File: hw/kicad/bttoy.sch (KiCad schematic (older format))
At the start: 29 parts

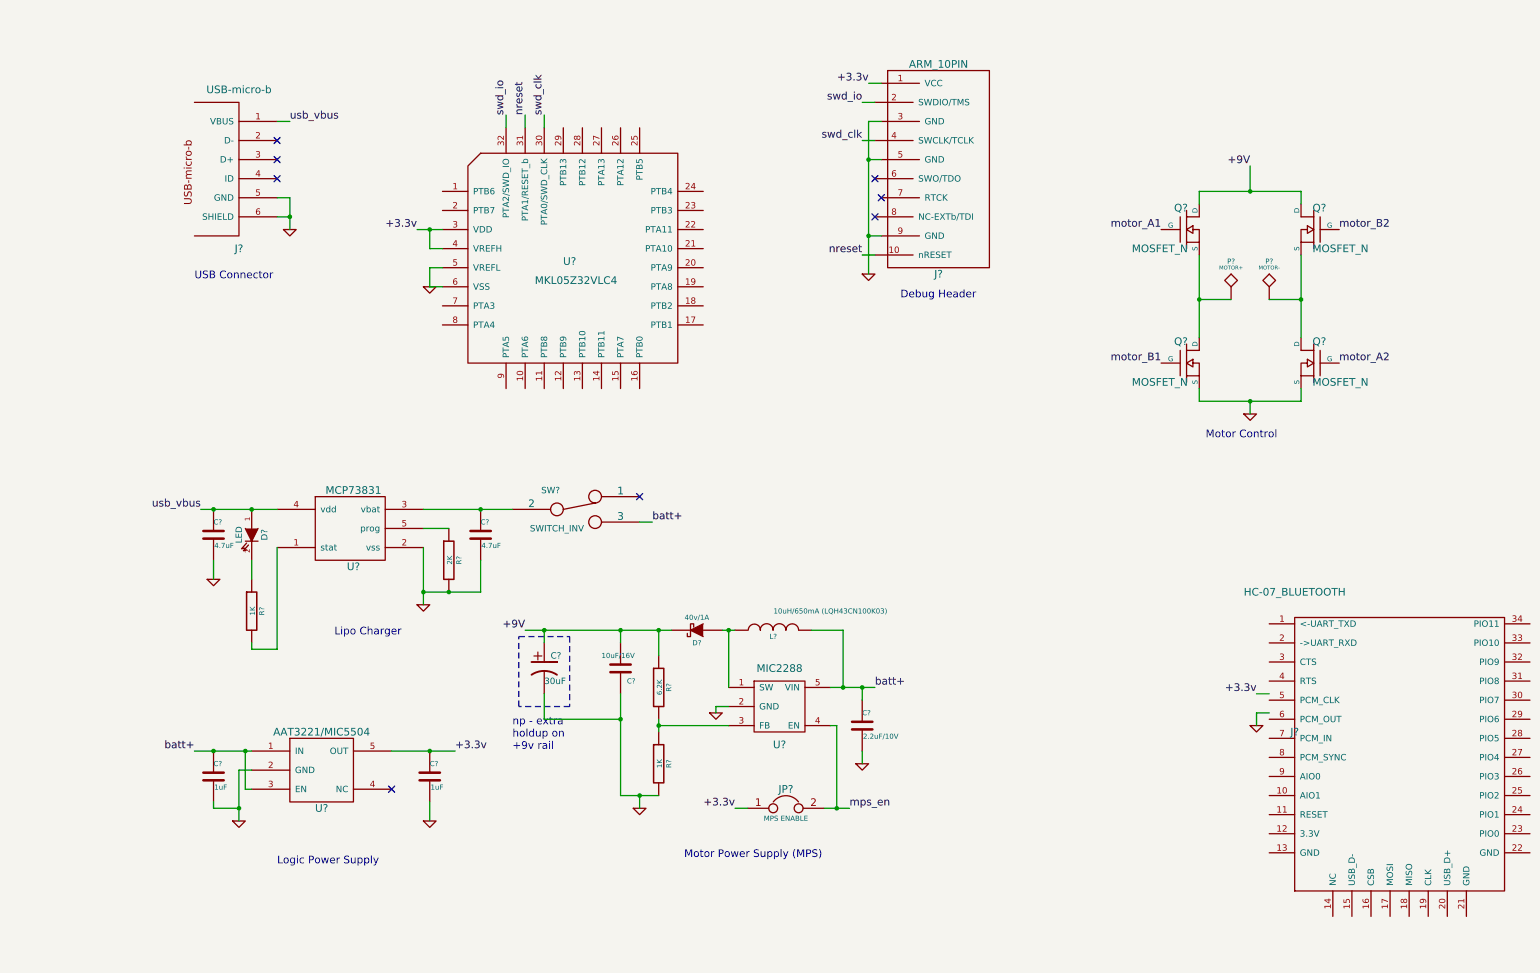
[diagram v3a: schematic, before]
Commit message: - change high side switches to pfet
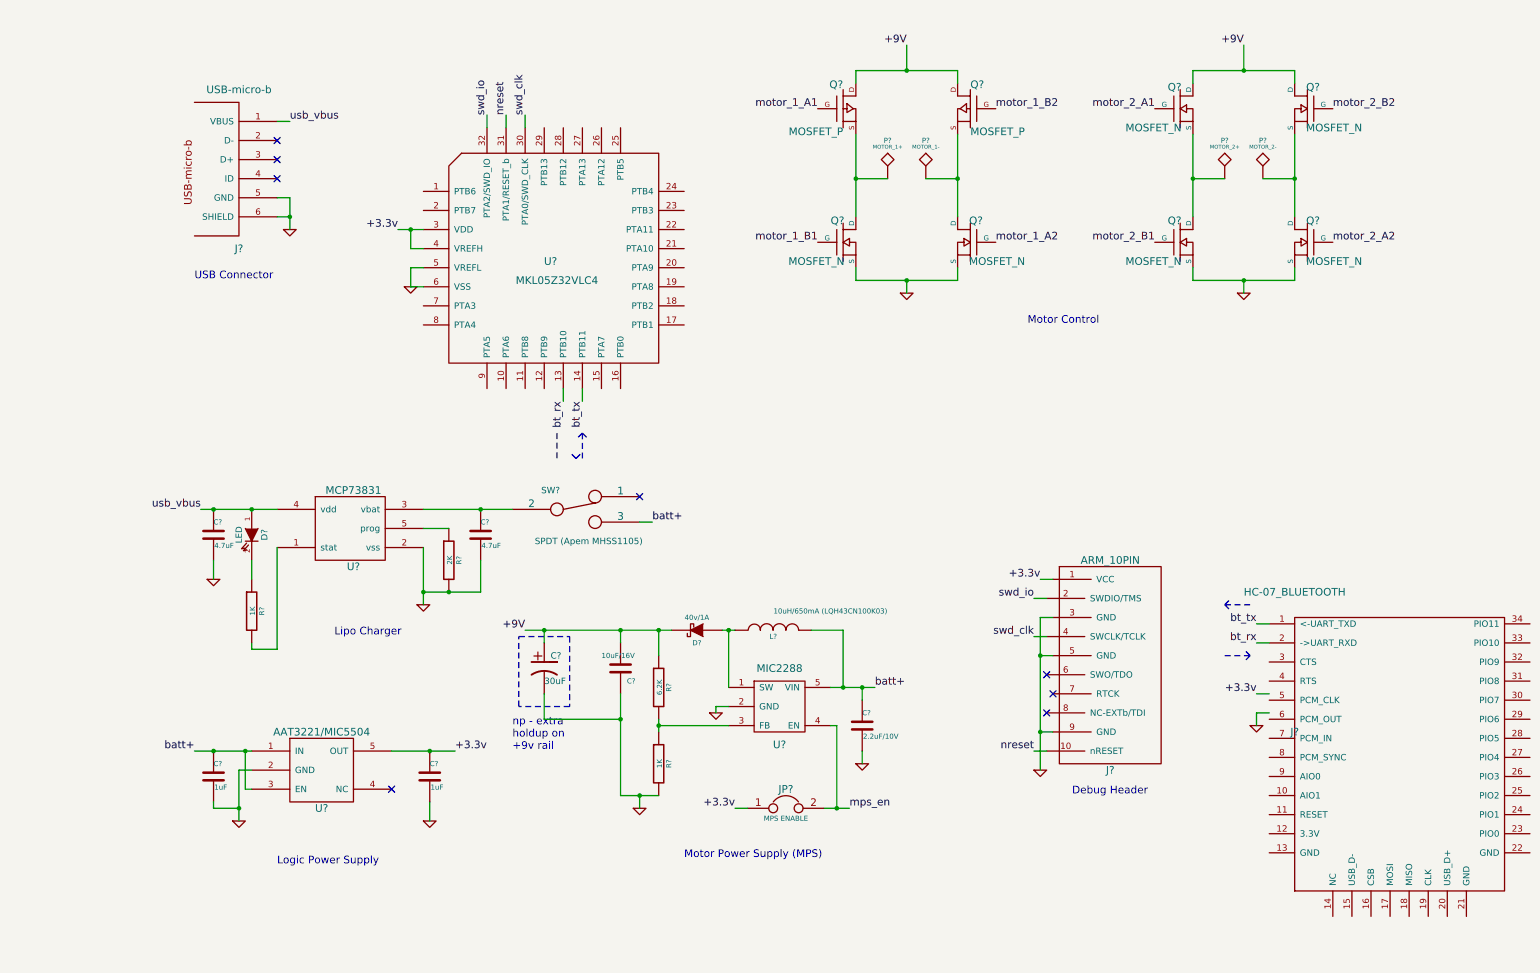
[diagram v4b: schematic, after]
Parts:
- added P?: MOTOR_1+, symbol TST
- added P?: MOTOR_1-, symbol TST
- added Q? (x2): MOSFET_N, symbol MOSFET_N
- added Q? (x2): MOSFET_P, symbol MOSFET_P
- P?: value MOTOR+ -> MOTOR_2+
- P?: value MOTOR- -> MOTOR_2-
- SW?: value SWITCH_INV -> SPDT (Apem MHSS1105)
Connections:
- net +9V: now also Q?.D, Q?.D
- net GND: now also Q?.S, Q?.S
- net bt_rx: now reaches U?.13 (PTB10)
- net bt_rx: now also J?.2 (->UART_RXD)
- net bt_tx: now reaches U?.14 (PTB11)
- net bt_tx: now also J?.1 (<-UART_TXD)
- net motor_A1 renamed motor_2_A1
- net motor_A2 renamed motor_2_A2
- net motor_B1 renamed motor_2_B1
- net motor_B2 renamed motor_2_B2
- new net: P?.1, Q?.D, Q?.S (x2)
- new net motor_1_A1: Q?.G
- new net motor_1_A2: Q?.G
- new net motor_1_B1: Q?.G
- new net motor_1_B2: Q?.G
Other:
- moved on the sheet: J?, P?, Q?, U?

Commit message: - remove sub schematic, replace discrete motor control with LV8548 IC
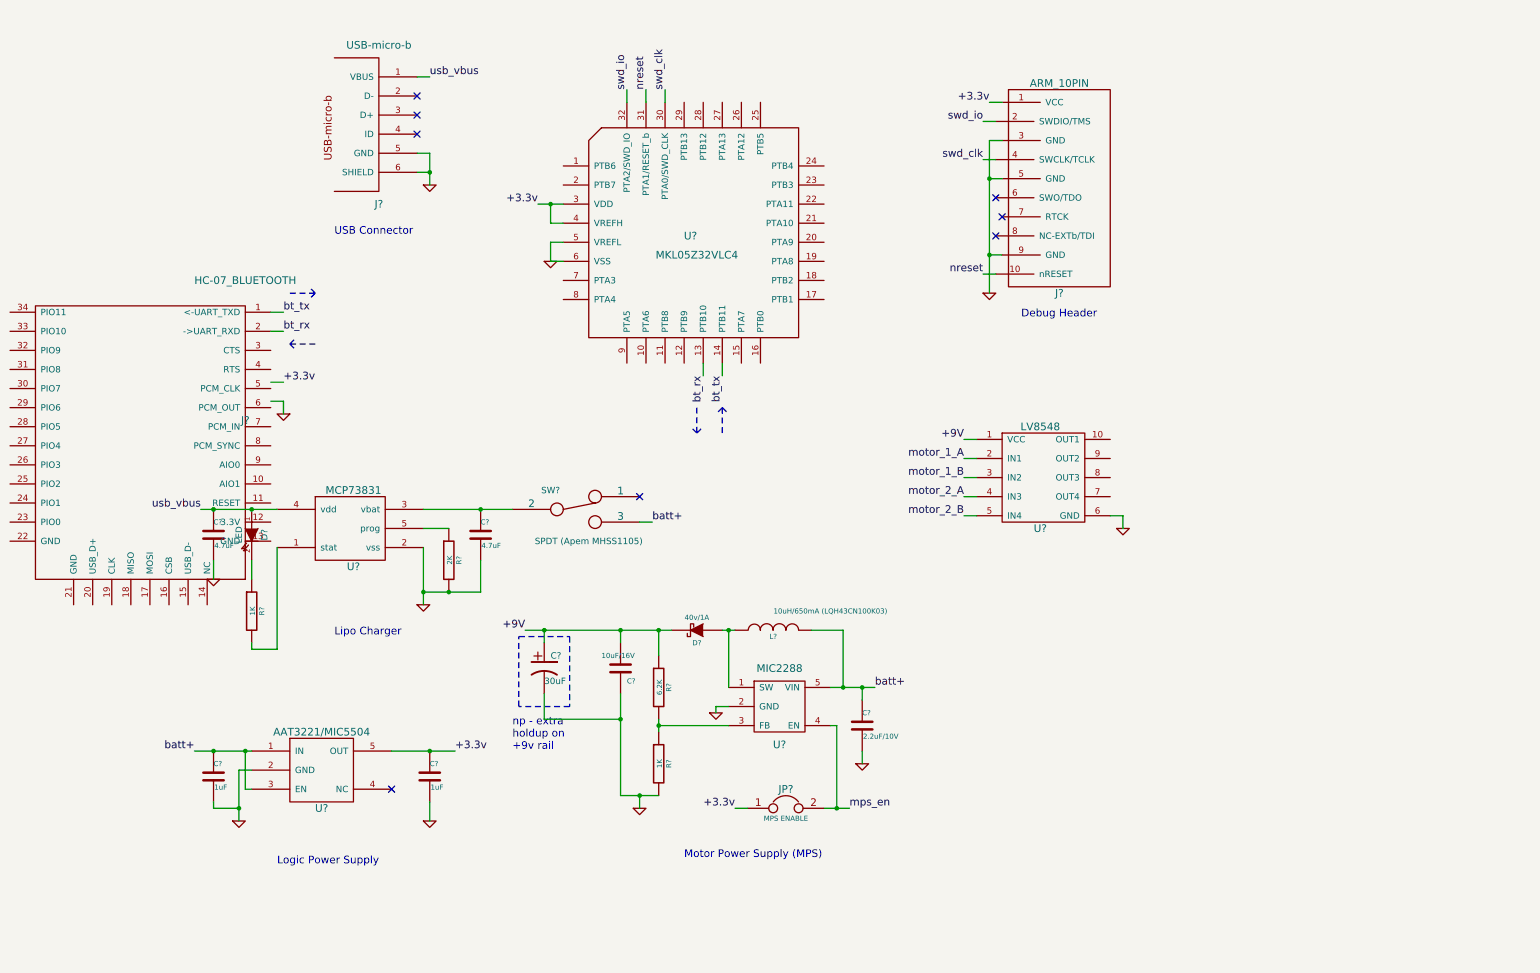
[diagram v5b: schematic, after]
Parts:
- removed P?: MOTOR_2+, symbol TST
- removed P?: MOTOR_2-, symbol TST
- removed P?: MOTOR_1+, symbol TST
- removed P?: MOTOR_1-, symbol TST
- removed Q? (x6): MOSFET_N, symbol MOSFET_N
- removed Q? (x2): MOSFET_P, symbol MOSFET_P
- added U?: LV8548, symbol LV8548
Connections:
- net +9V: now also U?.1 (VCC)
- net GND: now also U?.6 (GND)
- new net motor_1_A: U?.2 (IN1)
- new net motor_1_B: U?.3 (IN2)
- new net motor_2_A: U?.4 (IN3)
- new net motor_2_B: U?.5 (IN4)
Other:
- note removed: "Motor Control"
- moved on the sheet: J?, U?

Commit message: - add motor connectors
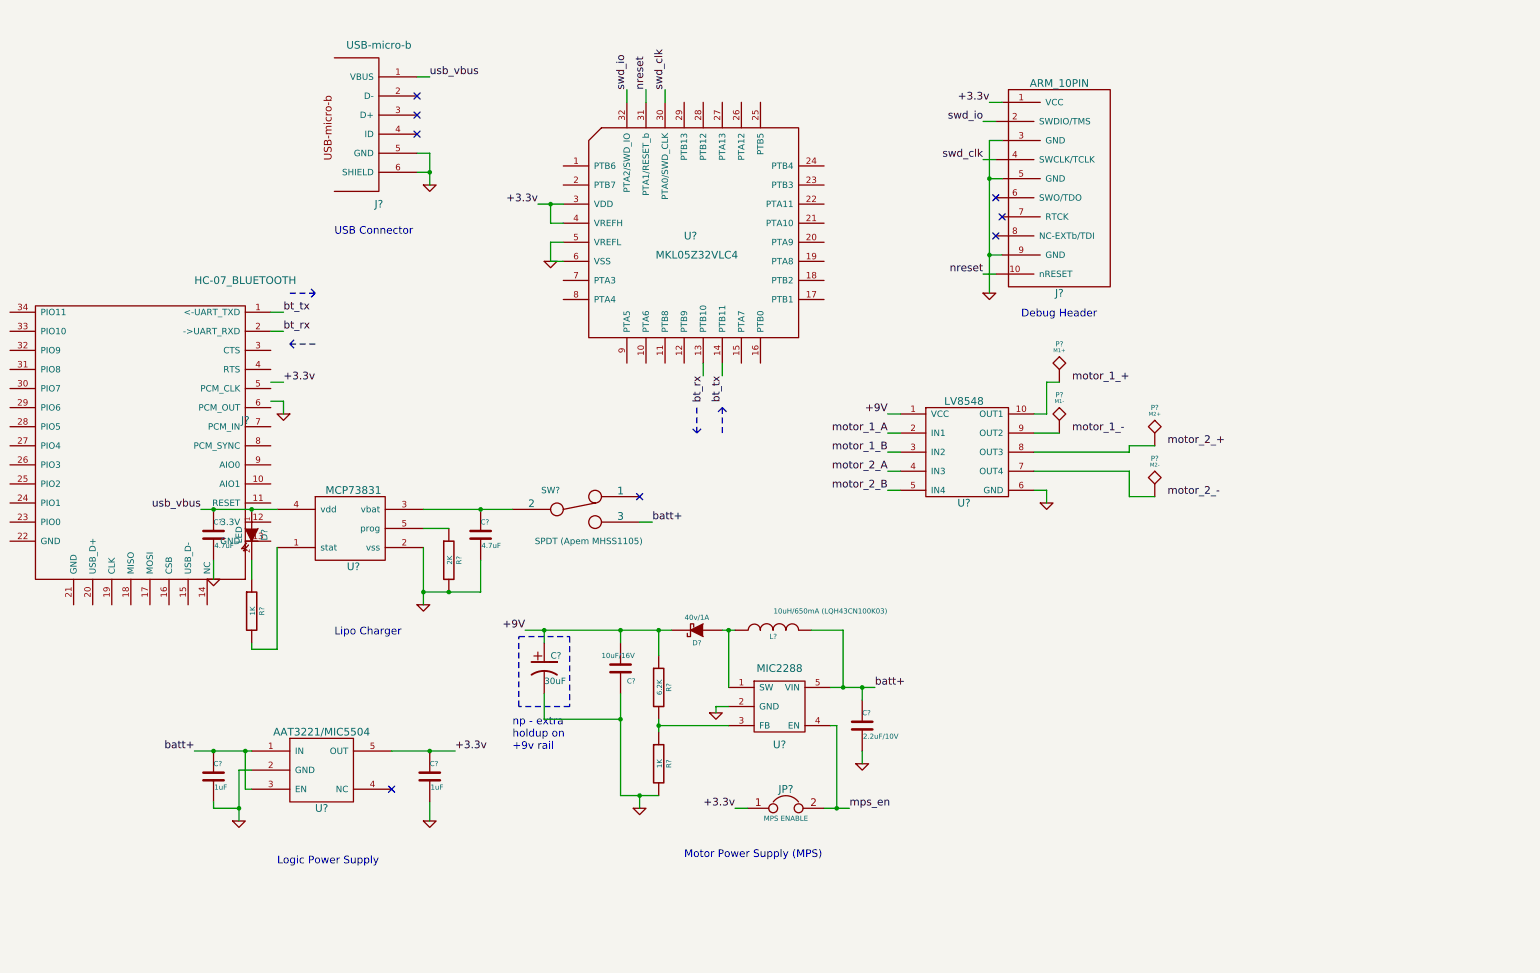
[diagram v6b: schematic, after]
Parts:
- added P?: M1+, symbol TST
- added P?: M1-, symbol TST
- added P?: M2+, symbol TST
- added P?: M2-, symbol TST
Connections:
- net at U?.10 (OUT1): now also P?.1
- net at U?.7 (OUT4): now also P?.1
- net at U?.8 (OUT3): now also P?.1
- net at U?.9 (OUT2): now also P?.1
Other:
- moved on the sheet: U?
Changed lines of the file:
@@
 	1    0    0    -1
 $EndComp
-Text Label 6950 4200 2    60   ~ 0
+Text Label 6350 4000 2    60   ~ 0
 motor_2_A
-Text Label 6950 4350 2    60   ~ 0
+Text Label 6350 4150 2    60   ~ 0
 motor_2_B
 $Comp
@@
 Text Label 5050 3250 3    60   ~ 0
 bt_tx
-Text Label 6950 3900 2    60   ~ 0
+Text Label 6350 3700 2    60   ~ 0
 motor_1_A
-Text Label 6950 4050 2    60   ~ 0
+Text Label 6350 3850 2    60   ~ 0
 motor_1_B
 $Comp
 L LV8548 U?
 U 1 1 54FC62AA
-P 7550 4000
-F 0 "U?" H 7550 3550 60  0000 C CNN
-F 1 "LV8548" H 7550 4350 60  0000 C CNN
-F 2 "" H 7450 4000 60  0000 C CNN
-F 3 "" H 7450 4000 60  0000 C CNN
-	1    7550 4000
+P 6950 3800
+F 0 "U?" H 6950 3350 60  0000 C CNN
+F 1 "LV8548" H 6950 4150 60  0000 C CNN
+F 2 "" H 6850 3800 60  0000 C CNN
+F 3 "" H 6850 3800 60  0000 C CNN
+	1    6950 3800
 	1    0    0    -1
 $EndComp
@@
 L GND #PWR?
 U 1 1 54FC64F5
-P 8200 4450
-F 0 "#PWR?" H 8200 4450 30  0001 C CNN
-F 1 "GND" H 8200 4380 30  0001 C CNN
-F 2 "" H 8200 4450 60  0000 C CNN
-F 3 "" H 8200 4450 60  0000 C CNN
-	1    8200 4450
-	1    0    0    -1
-$EndComp
-Text Label 6950 3750 2    60   ~ 0
+P 7600 4250
+F 0 "#PWR?" H 7600 4250 30  0001 C CNN
+F 1 "GND" H 7600 4180 30  0001 C CNN
+F 2 "" H 7600 4250 60  0000 C CNN
+F 3 "" H 7600 4250 60  0000 C CNN
+	1    7600 4250
+	1    0    0    -1
+$EndComp
+Text Label 6350 3550 2    60   ~ 0
 +9V
 Wire Wire Line
@@
 	2900 4450 2700 4450
 Wire Wire Line
-	2700 4300 3400 4300
+	2700 4300 3150 4300
+Wire Wire Line
+	3150 4300 3400 4300
 Connection ~ 1350 4300
 Wire Wire Line
 	1050 4850 1050 4700
 Wire Wire Line
-	2700 4600 2700 5050
-Wire Wire Line
-	2700 4950 3150 4950
+	2700 4600 2700 4950
+Wire Wire Line
+	2700 4950 2700 5050
+Wire Wire Line
+	2700 4950 2900 4950
+Wire Wire Line
+	2900 4950 3150 4950
 Connection ~ 2700 4950
 Wire Wire Line
@@
 	2650 900  2750 900
 Wire Wire Line
-	2750 1500 2750 1750
+	2750 1500 2750 1650
+Wire Wire Line
+	2750 1650 2750 1750
 Wire Wire Line
 	2750 1650 2650 1650
@@
 Connection ~ 2750 1650
 Wire Wire Line
-	2450 6200 2950 6200
-Wire Wire Line
-	900  6200 1350 6200
-Wire Wire Line
-	1250 6350 1250 6750
+	2450 6200 2750 6200
+Wire Wire Line
+	2750 6200 2950 6200
+Wire Wire Line
+	900  6200 1050 6200
+Wire Wire Line
+	1050 6200 1300 6200
+Wire Wire Line
+	1300 6200 1350 6200
+Wire Wire Line
+	1250 6350 1250 6650
+Wire Wire Line
+	1250 6650 1250 6750
 Wire Wire Line
 	1250 6350 1350 6350
@@
 	3700 2350 3800 2350
 Wire Wire Line
-	3600 1900 3800 1900
+	3600 1900 3700 1900
+Wire Wire Line
+	3700 1900 3800 1900
 Wire Wire Line
 	7150 2300 7250 2300
 Wire Wire Line
-	7150 1400 7150 2600
+	7150 1400 7150 1700
+Wire Wire Line
+	7150 1700 7150 2300
+Wire Wire Line
+	7150 2300 7150 2600
 Wire Wire Line
 	7150 1700 7250 1700
@@
 	7100 2450 7200 2450
 Wire Wire Line
-	950  4300 1550 4300
+	950  4300 1050 4300
+Wire Wire Line
+	1050 4300 1350 4300
+Wire Wire Line
+	1350 4300 1550 4300
 Connection ~ 1050 4300
 Wire Wire Line
-	5900 5700 6250 5700
-Wire Wire Line
-	5050 5250 5150 5250
+	5900 5700 6000 5700
+Wire Wire Line
+	6000 5700 6150 5700
+Wire Wire Line
+	6150 5700 6250 5700
+Wire Wire Line
+	5050 5250 5100 5250
+Wire Wire Line
+	5100 5250 5150 5250
 Wire Wire Line
 	6150 5800 6150 5700
@@
 	6150 6300 6150 6200
 Wire Wire Line
-	3500 5250 4650 5250
-Wire Wire Line
-	4250 5750 4250 6550
+	3500 5250 3650 5250
+Wire Wire Line
+	3650 5250 4250 5250
+Wire Wire Line
+	4250 5250 4550 5250
+Wire Wire Line
+	4550 5250 4650 5250
+Wire Wire Line
+	4250 5750 4250 5950
+Wire Wire Line
+	4250 5950 4250 6550
 Wire Wire Line
 	4550 5250 4550 5450
@@
 	4250 5350 4250 5250
 Wire Wire Line
-	4550 5950 4550 6050
-Wire Wire Line
-	4250 6550 4550 6550
+	4550 5950 4550 6000
+Wire Wire Line
+	4550 6000 4550 6050
+Wire Wire Line
+	4250 6550 4400 6550
+Wire Wire Line
+	4400 6550 4550 6550
 Wire Wire Line
 	4400 6550 4400 6650
@@
 	5150 6650 5250 6650
 Wire Wire Line
-	5850 6650 6050 6650
+	5850 6650 5950 6650
+Wire Wire Line
+	5950 6650 6050 6650
 Wire Wire Line
 	5950 6650 5950 6000
@@
 	5050 3250 5050 3150
 Wire Wire Line
-	6950 3750 7050 3750
-Wire Wire Line
-	8100 4350 8200 4350
-Wire Wire Line
-	8200 4350 8200 4450
-Wire Wire Line
-	6950 3900 7050 3900
-Wire Wire Line
-	6950 4050 7050 4050
-Wire Wire Line
-	7050 4200 6950 4200
-Wire Wire Line
-	6950 4350 7050 4350
+	6350 3550 6450 3550
+Wire Wire Line
+	7500 4150 7600 4150
+Wire Wire Line
+	7600 4150 7600 4250
+Wire Wire Line
+	6350 3700 6450 3700
+Wire Wire Line
+	6350 3850 6450 3850
+Wire Wire Line
+	6450 4000 6350 4000
+Wire Wire Line
+	6350 4150 6450 4150
+$Comp
+L TST P?
+U 1 1 54FC793F
+P 7700 3300
+F 0 "P?" H 7700 3600 40  0000 C CNN
+F 1 "M1+" H 7700 3550 30  0000 C CNN
+F 2 "" H 7700 3300 60  0000 C CNN
+F 3 "" H 7700 3300 60  0000 C CNN
+	1    7700 3300
+	1    0    0    -1
+$EndComp
+Text Label 7800 3300 0    60   ~ 0
+motor_1_+
+Text Label 7800 3700 0    60   ~ 0
+motor_1_-
+Text Label 8550 3800 0    60   ~ 0
+motor_2_+
+Text Label 8550 4200 0    60   ~ 0
+motor_2_-
+$Comp
+L TST P?
+U 1 1 54FC7D5F
+P 7700 3700
+F 0 "P?" H 7700 4000 40  0000 C CNN
+F 1 "M1-" H 7700 3950 30  0000 C CNN
+F 2 "" H 7700 3700 60  0000 C CNN
+F 3 "" H 7700 3700 60  0000 C CNN
+	1    7700 3700
+	1    0    0    -1
+$EndComp
+$Comp
+L TST P?
+U 1 1 54FC7D8F
+P 8450 3800
+F 0 "P?" H 8450 4100 40  0000 C CNN
+F 1 "M2+" H 8450 4050 30  0000 C CNN
+F 2 "" H 8450 3800 60  0000 C CNN
+F 3 "" H 8450 3800 60  0000 C CNN
+	1    8450 3800
+	1    0    0    -1
+$EndComp
+$Comp
+L TST P?
+U 1 1 54FC7DC0
+P 8450 4200
+F 0 "P?" H 8450 4500 40  0000 C CNN
+F 1 "M2-" H 8450 4450 30  0000 C CNN
+F 2 "" H 8450 4200 60  0000 C CNN
+F 3 "" H 8450 4200 60  0000 C CNN
+	1    8450 4200
+	1    0    0    -1
+$EndComp
+Wire Wire Line
+	7500 3550 7600 3550
+Wire Wire Line
+	7600 3550 7600 3300
+Wire Wire Line
+	7600 3300 7700 3300
+Wire Wire Line
+	7500 3700 7700 3700
+Wire Wire Line
+	7500 3850 8250 3850
+Wire Wire Line
+	8250 3850 8250 3800
+Wire Wire Line
+	8250 3800 8450 3800
+Wire Wire Line
+	7500 4000 8250 4000
+Wire Wire Line
+	8250 4000 8250 4200
+Wire Wire Line
+	8250 4200 8450 4200
 $EndSCHEMATC
